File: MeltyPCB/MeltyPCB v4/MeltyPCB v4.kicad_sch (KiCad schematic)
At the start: 19 parts, among them U0 Teensy 4.0, U1 XIAO_ESP32_S3

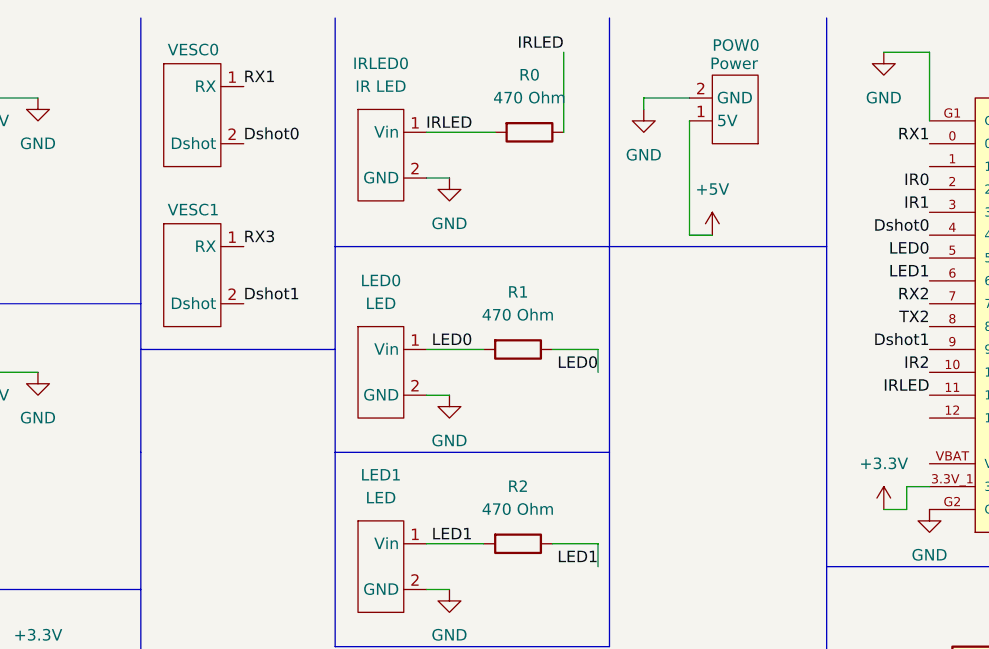
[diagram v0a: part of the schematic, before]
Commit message: Updated MeltyPCB v4 + Kicad Libraries
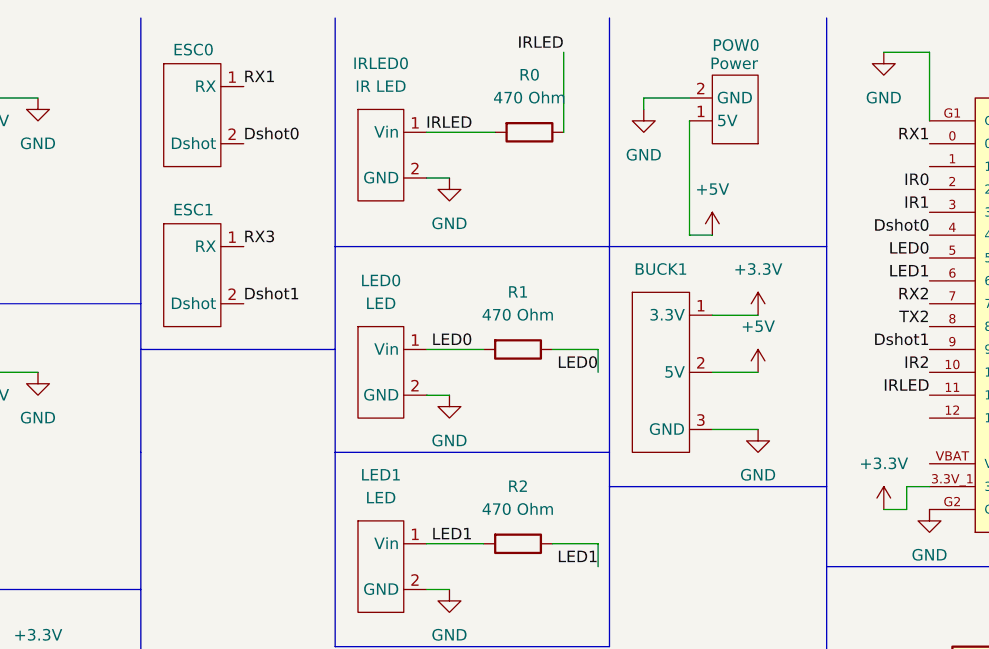
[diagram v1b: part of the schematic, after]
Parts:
- added BUCK1: (no value), MeltyPCB:Buck Converter, symbol MeltyPCB:Buck Converter
- U0: footprint Teensy_4.0:Teensy 4.0 (Simplified) -> Teensy_4.0:Teensy 4.0 (Simplified) (Extra Holes)
- U1: footprint XIAO_ESP32_S3:MODULE_XIAO_ESP32_S3 -> XIAO_ESP32_S3:XIAO_ESP32_S3 (Extra Holes)
- renumbered VESC0 to ESC0, VESC1 to ESC1
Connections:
- net +3.3V: now also BUCK1.1 (3.3V)
- net +5V: now also BUCK1.2 (5V)
- net GND: now also BUCK1.3 (GND)
